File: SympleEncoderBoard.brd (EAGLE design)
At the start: 160 x 100 mm, 1 part, among them Y1 CSTCE12M0G55-_R0

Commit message: ライブラリとかバスを作っただけ
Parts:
- removed Y1: CSTCE12M0G55-_R0, SympleEncoderBoard:CRYSTAL
- added IC1: STM32F446RET6, STM32F446RET6:QFP50P1200X1200X160-64N
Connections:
- new net VCP_RX: IC1.17
- new net VCP_TX: IC1.16
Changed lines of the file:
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@@
 </autorouter>
 <elements>
-<element name="Y1" library="SympleEncoderBoard" package="CRYSTAL" value="CSTCE12M0G55-_R0" x="-24.13" y="2.54" smashed="yes"/>
+<element name="IC1" library="STM32F446RET6" package="QFP50P1200X1200X160-64N" value="STM32F446RET6" x="7.62" y="-7.62" smashed="yes">
+<attribute name="DESCRIPTION" value="32-Bit MCU+DSP 512K Flash 180MHz LQFP64 STMicroelectronics STM32F446RET6, 32bit ARM Cortex M4 MCU, 180MHz, 512 kB Flash, 64-Pin LQFP" x="7.62" y="-7.62" size="1.778" layer="27" display="off"/>
+<attribute name="HEIGHT" value="1.6mm" x="7.62" y="-7.62" size="1.778" layer="27" display="off"/>
+<attribute name="MANUFACTURER_NAME" value="STMicroelectronics" x="7.62" y="-7.62" size="1.778" layer="27" display="off"/>
+<attribute name="MANUFACTURER_PART_NUMBER" value="STM32F446RET6" x="7.62" y="-7.62" size="1.778" layer="27" display="off"/>
+<attribute name="NAME" x="7.62" y="-7.62" size="1.27" layer="25" align="center"/>
+<attribute name="RS_PART_NUMBER" value="1106621P" x="7.62" y="-7.62" size="1.778" layer="27" display="off"/>
+<attribute name="RS_PRICE-STOCK" value="http://uk.rs-online.com/web/p/products/1106621P" x="7.62" y="-7.62" size="1.778" layer="27" display="off"/>
+<attribute name="VALUE" x="7.62" y="-7.62" size="1.27" layer="27" align="center"/>
+</element>
 </elements>
 <signals>
+<signal name="VCP_RX">
+<contactref element="IC1" pad="17"/>
+</signal>
+<signal name="VCP_TX">
+<contactref element="IC1" pad="16"/>
+</signal>
 </signals>
 <mfgpreviewcolors>

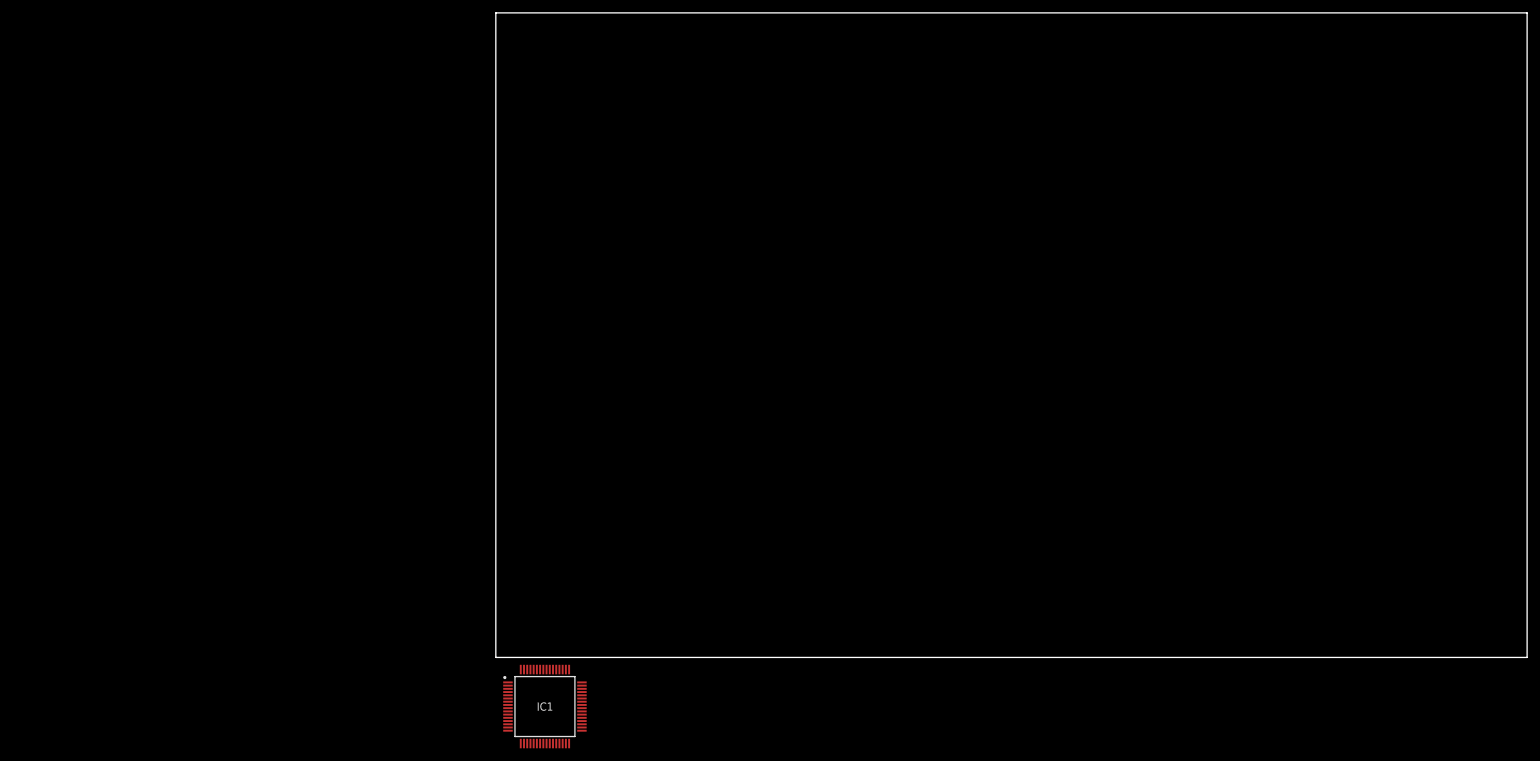
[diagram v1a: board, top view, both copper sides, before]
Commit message: 回路図は完成、コネクタつけた
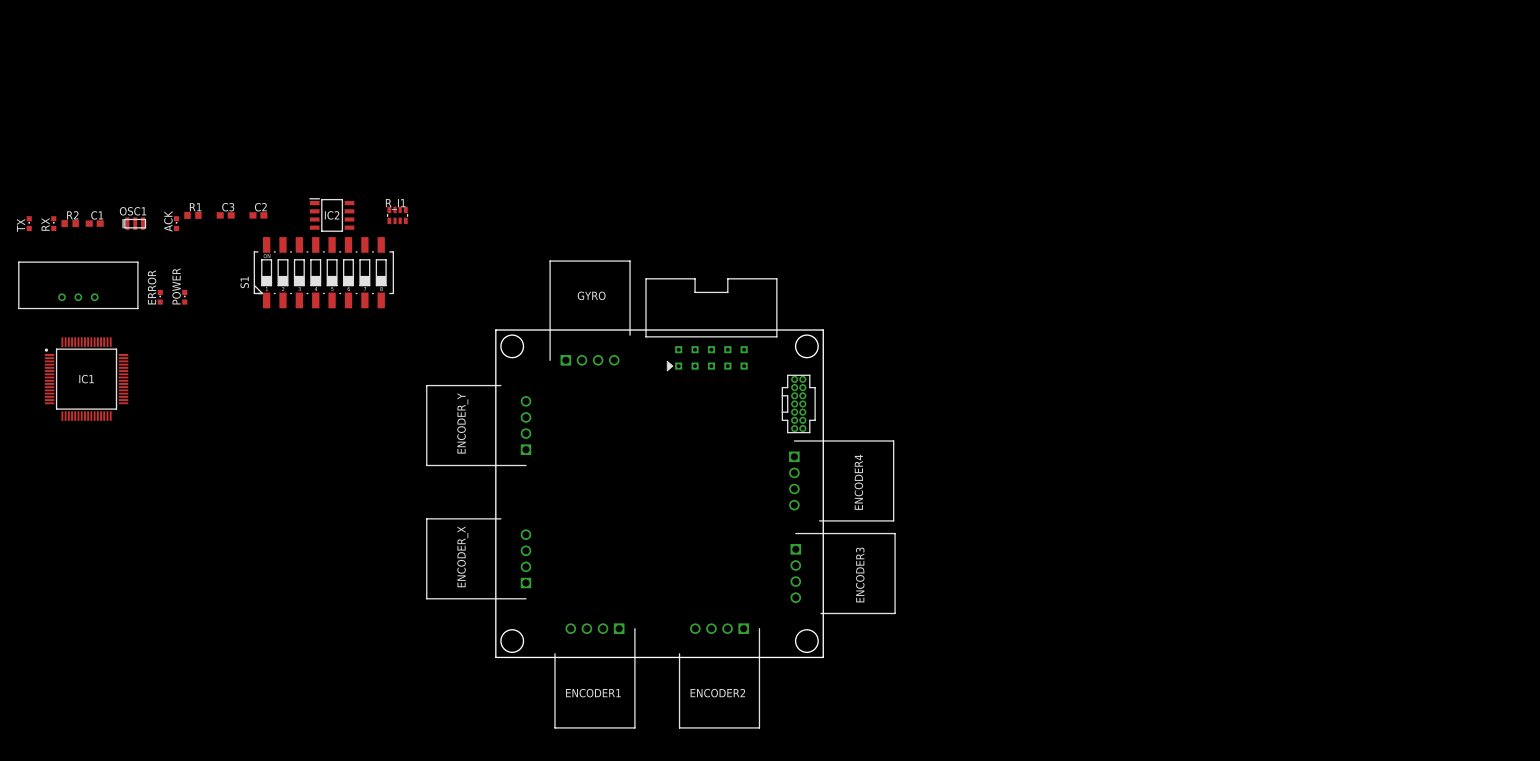
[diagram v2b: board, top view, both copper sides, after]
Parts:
- added ACK, ERROR, POWER, RX, TX: (no value), led:CHIPLED_0603
- added BOX10P-L1: BOX10PBOX10P-L, user_conector:BOX10P-L
- added C1: (no value), rcl:C1608
- added C2: 4.7μ, rcl:C0603
- added C3: 0.1μ, rcl:C0603
- added ENCODER1, ENCODER2, ENCODER3, ENCODER4, ENCODER_X, ENCODER_Y, GYRO: S4B-XH-A_LF__SN_, S4B-XH-A_LF__SN_:SHDRRA4W64P0X250_1X4_1240X1150
- added IC2: MCP2551-I_SN, MCP2551-I_SN:SOIC127P600X175-8N
- added OSC1: (no value), user_osc:CSTNE#
- added R1: 10k, rcl:R0603
- added R2: (no value), rcl:R0603
- added R_I1: 150, user_rcl:0603X4RESISTOR
- added S1: 219-08, switch-dil:CTS-219-08
- added U$1: BOX14P, user_conector:CON_HEDA14P_1.27
- added U$2: BP5293-33, SympleEncoderBoard:DC/DC_REGULATOR_3P
- moved IC1 87.4 mm to (-63.5, 43.2)
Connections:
- new net +12V: BOX10P-L1.P$10, BOX10P-L1.P$9, U$2.P$1
- new net +3.3V: C1.2, C3.1, IC1.1, IC1.13, IC1.19, POWER.A, U$1.3, U$2.P$3
- new net +5V: BOX10P-L1.P$1, BOX10P-L1.P$2, ENCODER1.4, ENCODER2.4, ENCODER3.4, ENCODER4.4, ENCODER_X.4, ENCODER_Y.4, GYRO.4, IC2.3
- new net CAN_H: BOX10P-L1.P$6, IC2.7
- new net CAN_L: BOX10P-L1.P$5, IC2.6
- new net CAN_RX: IC1.44, IC2.4
- new net CAN_TX: IC1.45, IC2.1
- new net EN1_A: ENCODER1.3, IC1.22
- new net EN1_B: ENCODER1.2, IC1.23
- new net EN2_A: ENCODER2.3, IC1.37
- new net EN2_B: ENCODER2.2, IC1.38
- new net EN3_A: ENCODER3.3, IC1.41
- new net EN3_B: ENCODER3.2, IC1.42
- new net EN4_A: ENCODER4.3, IC1.58
- new net EN4_B: ENCODER4.2, IC1.59
- new net ENX_A: ENCODER_X.3, IC1.21
- new net ENX_B: ENCODER_X.2, IC1.62
- new net ENY_A: ENCODER_Y.3, IC1.14
- new net ENY_B: ENCODER_Y.2, IC1.15
- new net ERRORLED: IC1.43, R_I1.8
- new net GND: ACK.C, BOX10P-L1.P$3, BOX10P-L1.P$4, C1.1, C2.2, C3.2, ENCODER1.1, ENCODER2.1, ENCODER3.1, ENCODER4.1, ENCODER_X.1, ENCODER_Y.1, ERROR.C, GYRO.1, IC1.12, IC1.18, IC1.31, IC1.47, IC1.63, IC2.2, OSC1.P$2, POWER.C, R1.2, R2.2, RX.C, S1.1, S1.2, S1.3, S1.4, S1.5, S1.6, S1.7, S1.8, TX.C, U$1.11, U$1.5, U$1.7, U$2.P$2
- new net I2C_SCL: GYRO.2, IC1.29
- new net I2C_SDA: GYRO.3, IC1.52
- new net LED1: IC1.40, R_I1.7
- new net LED2: IC1.39, R_I1.6
- new net LEDGYRO: IC1.61, R_I1.5
- new net N$1: IC1.60, R1.1
- new net N$2: C2.1, IC1.30
- new net N$3: ERROR.A, R_I1.1
- new net N$4: R_I1.2, TX.A
- new net N$5: RX.A, R_I1.3
- new net N$6: ACK.A, R_I1.4
- new net N$7: IC2.8, R2.1
- new net NRST: IC1.7, U$1.12
- new net OSC_IN: IC1.5, OSC1.P$1
- new net OSC_OUT: IC1.6, OSC1.P$3
- new net SW1: IC1.35, S1.9
- new net SW2: IC1.34, S1.10
- new net SW3: IC1.33, S1.11
- new net SW4: IC1.28, S1.12
- new net SW5: IC1.27, S1.13
- new net SW6: IC1.26, S1.14
- new net SW7: IC1.25, S1.15
- new net SW8: IC1.24, S1.16
- new net SWCLK: IC1.49, U$1.6
- new net SWDIO: IC1.46, U$1.4
- new net SWO: IC1.54, U$1.8
- net VCP_RX: now also U$1.13
- net VCP_TX: now also U$1.14
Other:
- board size 160 x 100 mm -> 50.8 x 50.8 mm

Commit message: 回路図書きました
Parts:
- added R3: 150, rcl:R0603
- R2: value (none) -> 33k
- moved TX 116.4 mm to (37.3, 28.4), turned to 270 degrees
- moved RX 112.1 mm to (37.3, 30.6), turned to 270 degrees
- moved U$2 99.5 mm to (33.8, 42.1), turned to 180 degrees
- moved R2 94.4 mm to (13.0, 15.7), turned to 180 degrees
- moved ERROR 94.1 mm to (37.1, 25.9), turned to 90 degrees
- moved ACK 93.5 mm to (37.3, 32.5), turned to 270 degrees
- moved POWER 91.6 mm to (37.1, 22.7), turned to 90 degrees
- moved IC1 83.2 mm to (18.5, 29.2)
- moved C1 80.6 mm to (14.2, 41.7), turned to 180 degrees
- moved S1 75.4 mm to (32.3, 12.7)
- moved C2 74.3 mm to (18.8, 19.4), turned to 180 degrees
- moved OSC1 73.0 mm to (7.31, 33.1), turned to 270 degrees
- moved R1 71.3 mm to (19.0, 41.6)
- moved IC2 70.7 mm to (13.6, 9.58)
- moved C3 65.1 mm to (7.42, 26.1), turned to 90 degrees
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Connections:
- new net N$8: POWER.A, R3.1
- net +3.3V: now also R3.2; no longer POWER.A
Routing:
- net GND: track 0.00 -> 279.8 mm, vias 0 -> 1
- net +5V: track 0.00 -> 131.5 mm
- net +3.3V: track 0.00 -> 113.3 mm, vias 0 -> 4
- net VCP_RX: track 0.00 -> 87.8 mm, vias 0 -> 1
- net CAN_L: track 0.00 -> 87.2 mm
- net VCP_TX: track 0.00 -> 59.5 mm, vias 0 -> 1
- net CAN_H: track 0.00 -> 57.9 mm, vias 0 -> 1
- net SW5: track 0.00 -> 57.4 mm, vias 0 -> 2
- net EN4_A: track 0.00 -> 54.4 mm, vias 0 -> 2
- net ENX_B: track 0.00 -> 45.2 mm
- net NRST: track 0.00 -> 42.0 mm, vias 0 -> 2
- net ENX_A: track 0.00 -> 37.3 mm, vias 0 -> 1
- net SWO: track 0.00 -> 37.0 mm
- net SWDIO: track 0.00 -> 35.2 mm, vias 0 -> 1
- net EN4_B: track 0.00 -> 33.7 mm
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
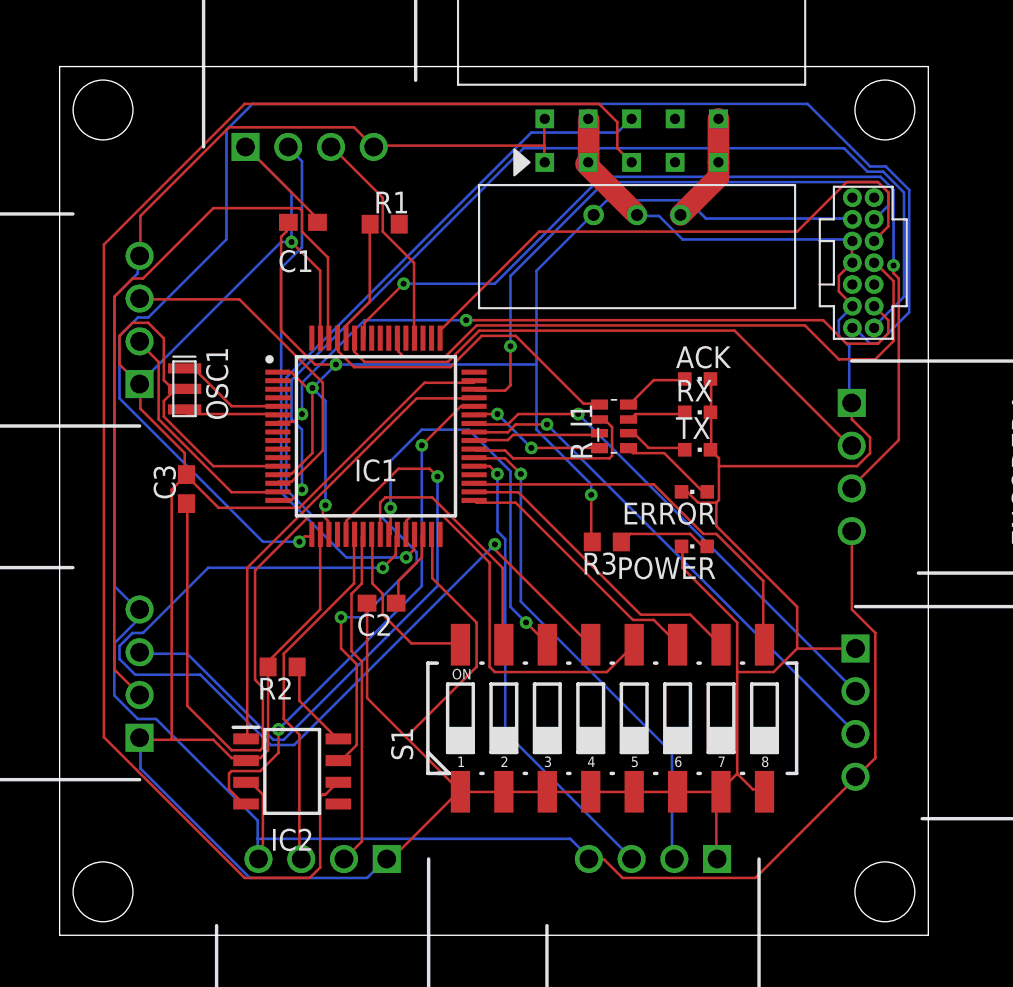
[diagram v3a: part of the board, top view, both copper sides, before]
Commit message: 10pboxのピンアサイン間違えてました
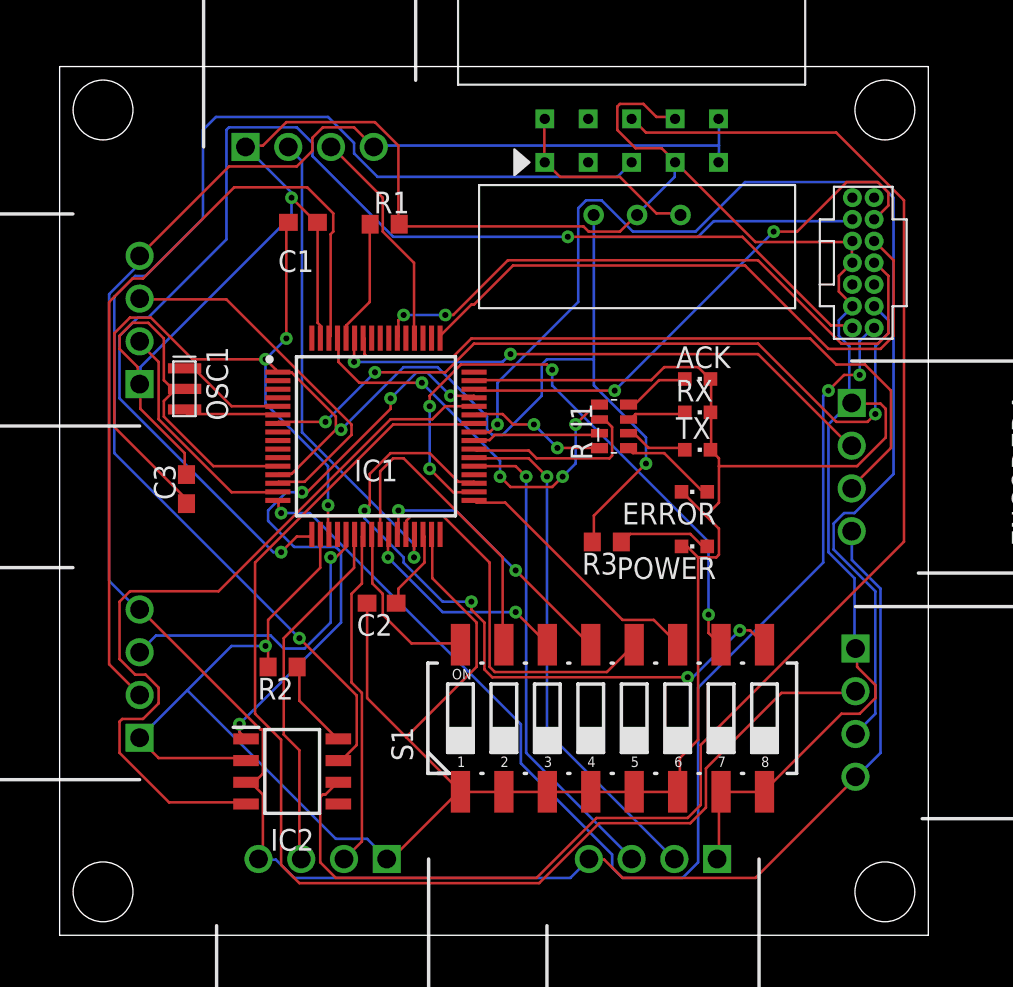
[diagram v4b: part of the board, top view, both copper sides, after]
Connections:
- net +12V: now also BOX10P-L1.P$1, BOX10P-L1.P$2; no longer BOX10P-L1.P$10, BOX10P-L1.P$9
- net +5V: now also BOX10P-L1.P$10, BOX10P-L1.P$9; no longer BOX10P-L1.P$1, BOX10P-L1.P$2
- net CAN_H: now also BOX10P-L1.P$5; no longer BOX10P-L1.P$6
- net CAN_L: now also BOX10P-L1.P$6; no longer BOX10P-L1.P$5
- net GND: now also BOX10P-L1.P$7, BOX10P-L1.P$8; no longer BOX10P-L1.P$3, BOX10P-L1.P$4
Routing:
- net EN3_B: track 29.3 -> 74.5 mm, vias 1 -> 0
- net EN3_A: track 30.0 -> 71.8 mm
- net SW5: track 57.4 -> 15.9 mm
- net GND: track 279.8 -> 301.4 mm, vias 1 -> 2
- net ENX_A: track 37.3 -> 18.2 mm
- net SW1: track 23.0 -> 40.9 mm, vias 0 -> 4
- net SW2: track 18.1 -> 35.7 mm, vias 0 -> 4
- net CAN_H: track 57.9 -> 73.4 mm
- net CAN_RX: track 31.2 -> 45.9 mm, vias 2 -> 0
- net EN4_A: track 54.4 -> 40.2 mm, vias 2 -> 0
- net VCP_TX: track 59.5 -> 72.3 mm, vias 1 -> 3
- net VCP_RX: track 87.8 -> 76.1 mm, vias 1 -> 2
- net SW6: track 24.2 -> 12.8 mm
- net CAN_TX: track 27.4 -> 35.6 mm, vias 0 -> 4
- net +12V: track 6.54 -> 11.8 mm
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
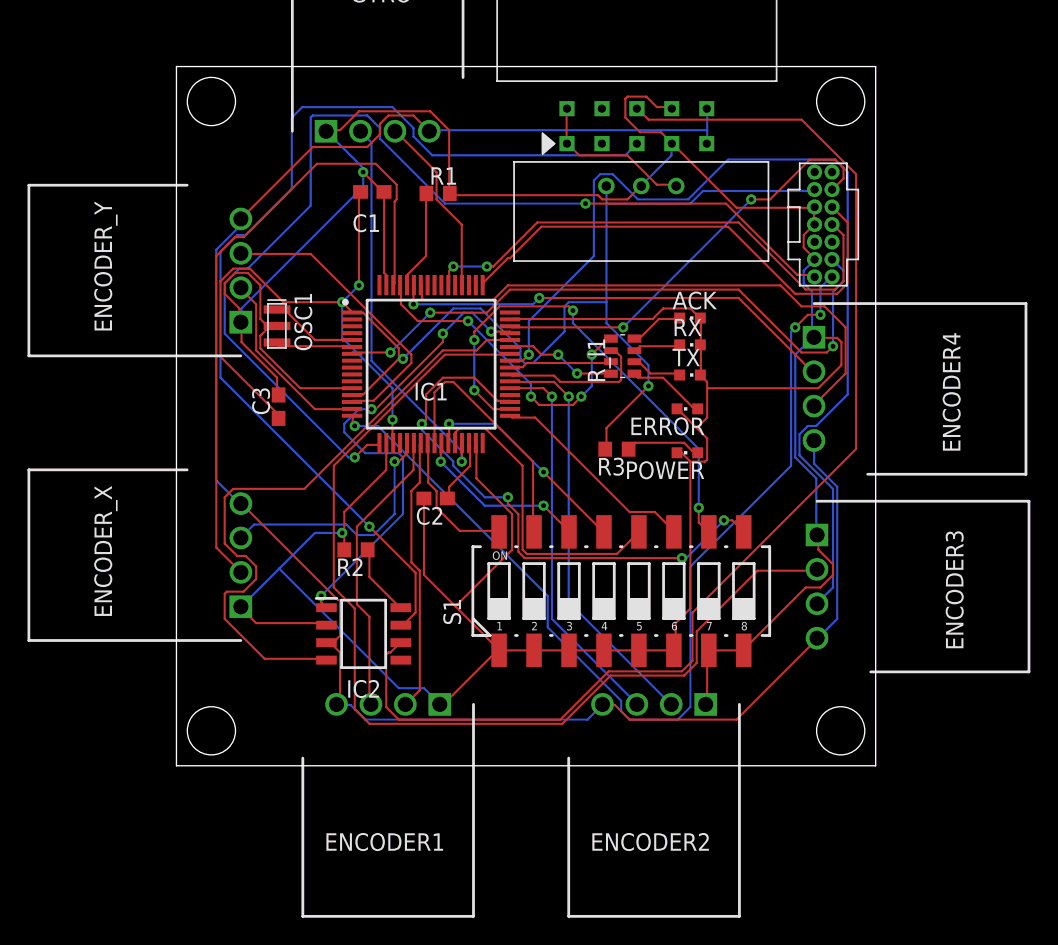
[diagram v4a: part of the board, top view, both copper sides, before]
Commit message: CANトランシーバの位置と型番更新、MLCC・VDD・VSS接続、配線太さ、14Pコネクタ配置変更
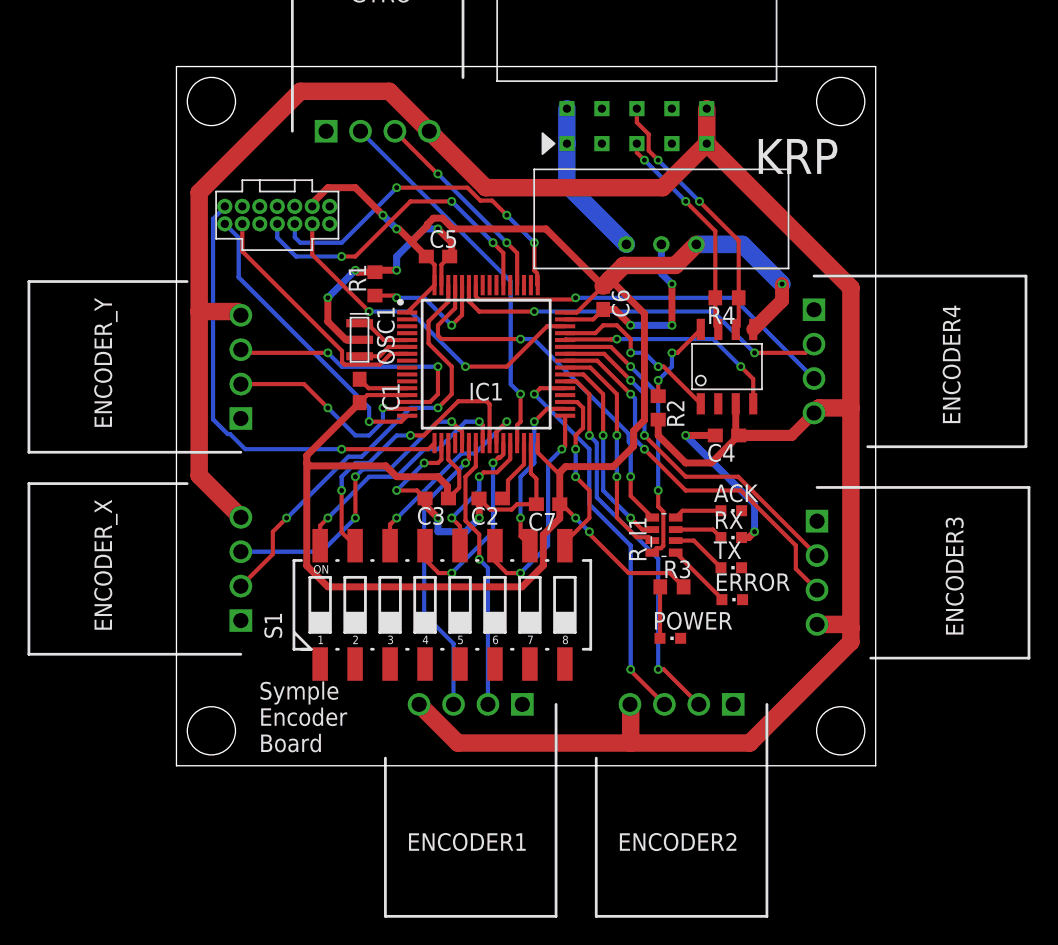
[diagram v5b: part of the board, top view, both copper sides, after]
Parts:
- removed IC2: MCP2551-I_SN, MCP2551-I_SN:SOIC127P600X175-8N
- added C4: 0.1μ, rcl:C1608
- added C5, C6, C7: 0.1μ, rcl:C0603
- added R4: 120, rcl:R0603
- added U$3: MCP2562MCP2561-SN, user_ic:SOIC8
- C1: value (none) -> 1μ
- R2: value 33k -> 10k
- moved U$1 42.9 mm to (2.88, 41.7), turned to 270 degrees
- moved R2 24.3 mm to (35.0, 26.0), turned to 270 degrees
- moved C1 14.5 mm to (13.3, 27.2), turned to 270 degrees
- moved ACK 14.3 mm to (40.3, 18.5)
- moved RX 14.3 mm to (40.3, 16.6)
- moved TX 14.3 mm to (40.3, 14.4)
- moved ERROR 14.2 mm to (40.4, 12.1), turned to 270 degrees
- moved POWER 13.5 mm to (35.9, 9.26), turned to 270 degrees
- moved R_I1 13.3 mm to (35.4, 16.8)
- moved C3 13.3 mm to (18.9, 19.4), turned to 180 degrees
- moved S1 13.0 mm to (19.3, 11.7)
- moved R3 10.8 mm to (36.0, 13.0), turned to 0 degrees
- moved R1 8.01 mm to (14.4, 35.0), turned to 90 degrees
- moved ENCODER_Y 7.00 mm to (4.68, 25.2)
- moved OSC1 6.08 mm to (13.3, 32.1)
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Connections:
- net +3.3V: now also C5.1, C6.1, C7.1, IC1.32, IC1.48, IC1.64, U$3.P$5
- net +5V: now also C4.1, R2.2, U$3.P$3; no longer IC2.3
- net CAN_H: now also R4.2, U$3.P$7; no longer IC2.7
- net CAN_L: now also R4.1, U$3.P$6; no longer IC2.6
- net CAN_RX: now also U$3.P$4; no longer IC2.4
- net CAN_TX: now also U$3.P$1; no longer IC2.1
- net GND: now also C4.2, C5.2, C6.2, C7.2, U$3.P$2; no longer IC2.2, R2.2
- net N$7: now also U$3.P$8; no longer IC2.8
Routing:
- net GND: track 301.4 -> 75.6 mm, vias 2 -> 13
- net CAN_L: track 87.8 -> 19.2 mm, vias 0 -> 2
- net CAN_H: track 73.4 -> 16.0 mm, vias 1 -> 2
- net VCP_TX: track 72.3 -> 21.7 mm, vias 3 -> 1
- net EN3_B: track 74.5 -> 26.1 mm, vias 0 -> 2
- net EN3_A: track 71.8 -> 28.0 mm, vias 1 -> 2
- net VCP_RX: track 76.1 -> 33.0 mm, vias 2 -> 1
- net +5V: track 136.3 -> 176.2 mm
- net +3.3V: track 112.0 -> 149.6 mm
- net CAN_RX: track 45.9 -> 16.7 mm, vias 0 -> 2
- net SW1: track 40.9 -> 12.9 mm, vias 4 -> 2
- net NRST: track 45.9 -> 18.2 mm, vias 3 -> 0
- net SW2: track 35.7 -> 12.3 mm, vias 4 -> 2
- net CAN_TX: track 35.6 -> 13.0 mm, vias 4 -> 2
- net ENX_B: track 47.6 -> 31.3 mm, vias 0 -> 2
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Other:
- board text added: "KRP"
- board text added: "Symple Encoder Board"
